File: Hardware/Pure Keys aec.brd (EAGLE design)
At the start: 97.8 x 98.7 mm, 58 parts, among them IC1 TL074P, IC2 TL072P, IC5 TL074P, Q2 20MHz, T1 2N3904, U2 LM4040A50IDBZT, U3 328P

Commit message: Slight update
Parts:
- removed U$6, U$7: PB6149L-5, INSTRUO:PB6149L
- added BUT1, BUT2: PB6149L-5, INSTRUO:PB6149L
- moved C10 60.8 mm to (20.3, 53.3)
- moved C18 45.8 mm to (29.2, 49.5)
- moved C7 44.5 mm to (86.4, 50.8), turned to 0 degrees
- moved C8 42.6 mm to (82.5, 50.8)
- moved Q2 39.9 mm to (31.8, 43.2), turned to 0 degrees
- moved U3 38.6 mm to (41.9, 58.4)
- moved C5 37.5 mm to (67.3, 34.3), turned to 0 degrees
- moved U$1 35.7 mm to (80.0, 43.2)
- moved C16 34.1 mm to (24.1, 49.5)
- moved C14 33.0 mm to (47.0, 78.7)
- moved C13 30.6 mm to (50.8, 78.7)
- moved C17 29.3 mm to (33.0, 49.5)
- moved R20 29.3 mm to (26.7, 82.5), turned to 0 degrees
- moved IC5 29.2 mm to (80.0, 27.9)
- moved C12 28.5 mm to (20.3, 64.8)
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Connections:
- removed net +UB: V1.16, V2.16
- removed net -UB: V1.8, V2.8
- removed net CLK_OUT: U3.14
- removed net MK5: V2.14
- net 5V: now also BUT1.3, BUT1.4, BUT2.3, BUT2.4, V1.16, V2.16; no longer U$6.3, U$6.4, U$7.3, U$7.4
- net BUT1: now also BUT1.1, BUT1.2; no longer U$7.1, U$7.2
- net BUT2: now also BUT2.1, BUT2.2; no longer U$6.1, U$6.2
- net BUTLED1: now also BUT1.A, U3.14; no longer U$7.A
- net BUTLED2: now also BUT2.A; no longer U$6.A
- net GND: now also V1.8, V2.14, V2.8
- net N$65: now also BUT1.K; no longer U$7.K
- net N$8: now also BUT2.K; no longer U$6.K
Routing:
- net CLK_IN: track 37.9 -> 102.1 mm
- net MOSI: track 146.7 -> 103.6 mm, vias 2 -> 0
- net POT2: track 25.3 -> 67.2 mm, vias 0 -> 1
- net BUTLED1: track 0.00 -> 39.1 mm
- net POT1: track 41.2 -> 78.7 mm
- net N$7: track 35.6 -> 69.2 mm
- net +UB: track 33.1 -> 0.00 mm
- net -UB: track 32.5 -> 0.00 mm
- net N$4: track 43.5 -> 74.6 mm
- net 5V: track 476.7 -> 505.4 mm
- net TRIG4: track 57.6 -> 29.2 mm, vias 0 -> 1
- net A1OUT: track 98.3 -> 71.7 mm, vias 1 -> 2
- net A2OUT: track 98.9 -> 74.0 mm
- net T6: track 55.6 -> 79.2 mm, vias 0 -> 2
- net N$36: track 17.5 -> 40.1 mm
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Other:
- board size 97.8 x 98.7 mm -> 99 x 98.7 mm

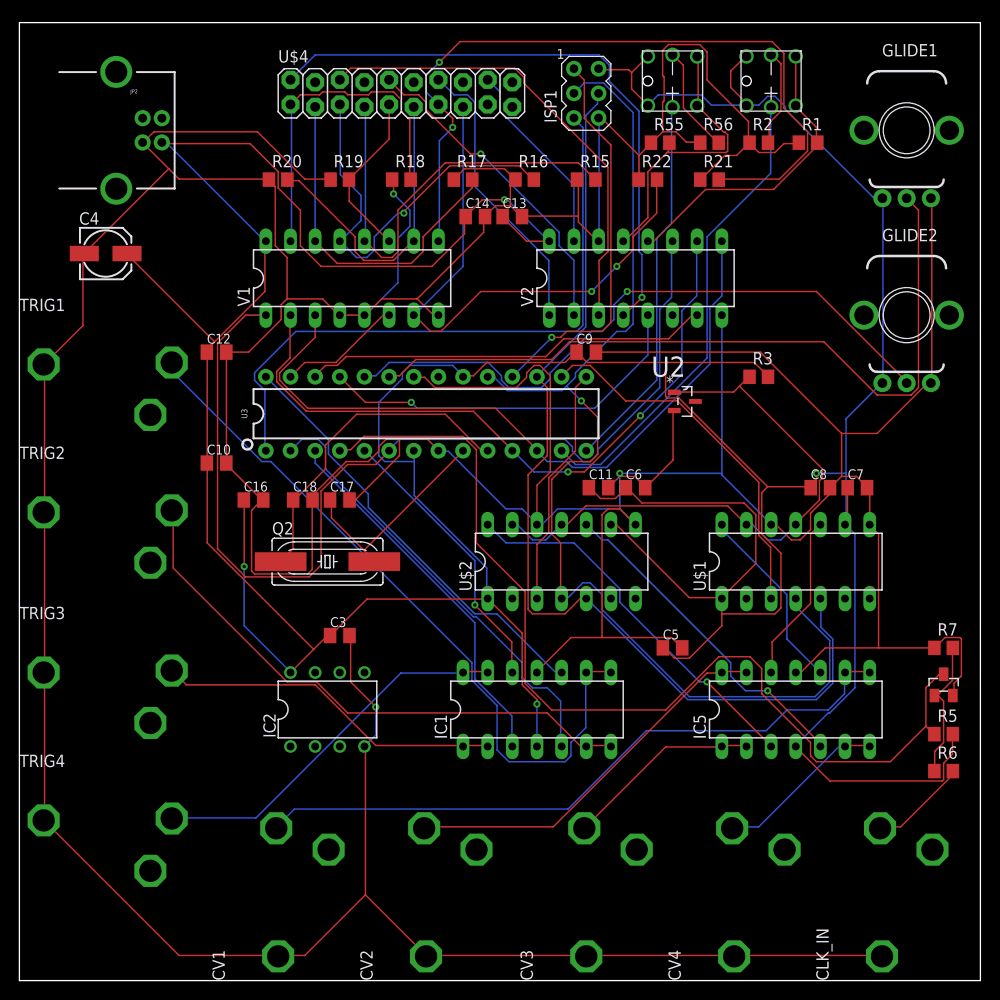
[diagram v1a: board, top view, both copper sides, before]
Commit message: Changed MUX/DEMUX connections and removed one POT
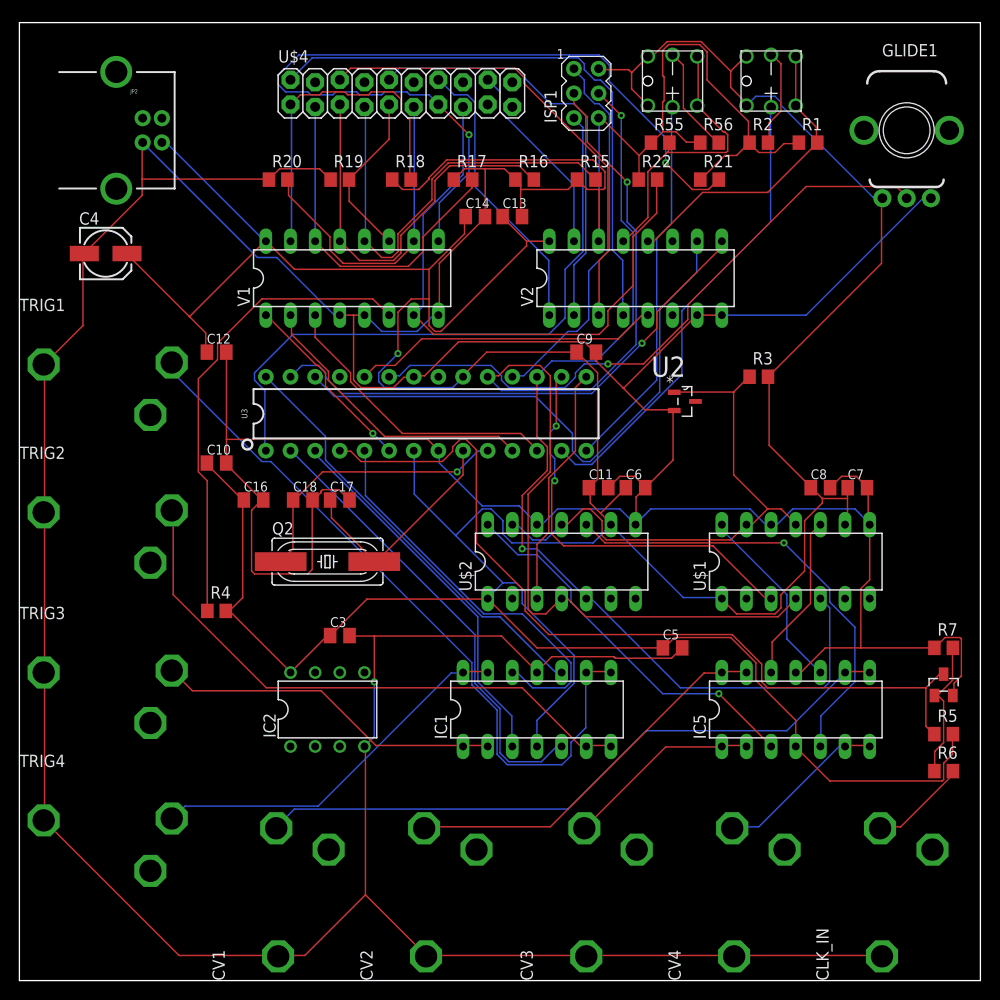
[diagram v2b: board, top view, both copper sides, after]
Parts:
- removed GLIDE2: rate, GMSN:POT
- added R4: 10K, rcl:R0805
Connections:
- removed net ENIN: U3.26, V2.7
- removed net POT2: GLIDE2.P$2, U3.24
- new net A0IN: U3.25
- new net A1IN: U3.26, V2.10
- new net A2IN: U3.27, V2.9
- new net AOIN: V2.11
- net 5V: now also R4.2; no longer GLIDE2.P$1
- net A0OUT: no longer V2.11
- net A1OUT: no longer V2.10
- net A2OUT: no longer V2.9
- net DAIN: now also U3.24; no longer U3.25
- net ENOUT: now also R4.1; no longer U3.27
- net GND: now also V2.7; no longer GLIDE2.P$3
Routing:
- net A0OUT: track 104.9 -> 19.3 mm, vias 0 -> 1
- net POT2: track 67.2 -> 0.00 mm, vias 1 -> 0
- net A1IN: track 0.00 -> 60.4 mm
- net 5V: track 505.4 -> 450.1 mm, vias 4 -> 1
- net A2IN: track 0.00 -> 54.2 mm, vias 0 -> 1
- net A2OUT: track 74.0 -> 30.6 mm
- net ENIN: track 42.1 -> 0.00 mm
- net A1OUT: track 71.7 -> 30.4 mm, vias 2 -> 0
- net ENOUT: track 12.8 -> 49.1 mm
- net GND: track 726.0 -> 700.2 mm, vias 3 -> 1
- net CLK_IN: track 102.1 -> 88.1 mm
- net POT1: track 78.7 -> 65.4 mm, vias 0 -> 1
- net TRIG4: track 29.2 -> 41.9 mm, vias 1 -> 0
- net VOUTD: track 34.6 -> 46.6 mm
- net T6: track 79.2 -> 90.5 mm
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
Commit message: added back plane
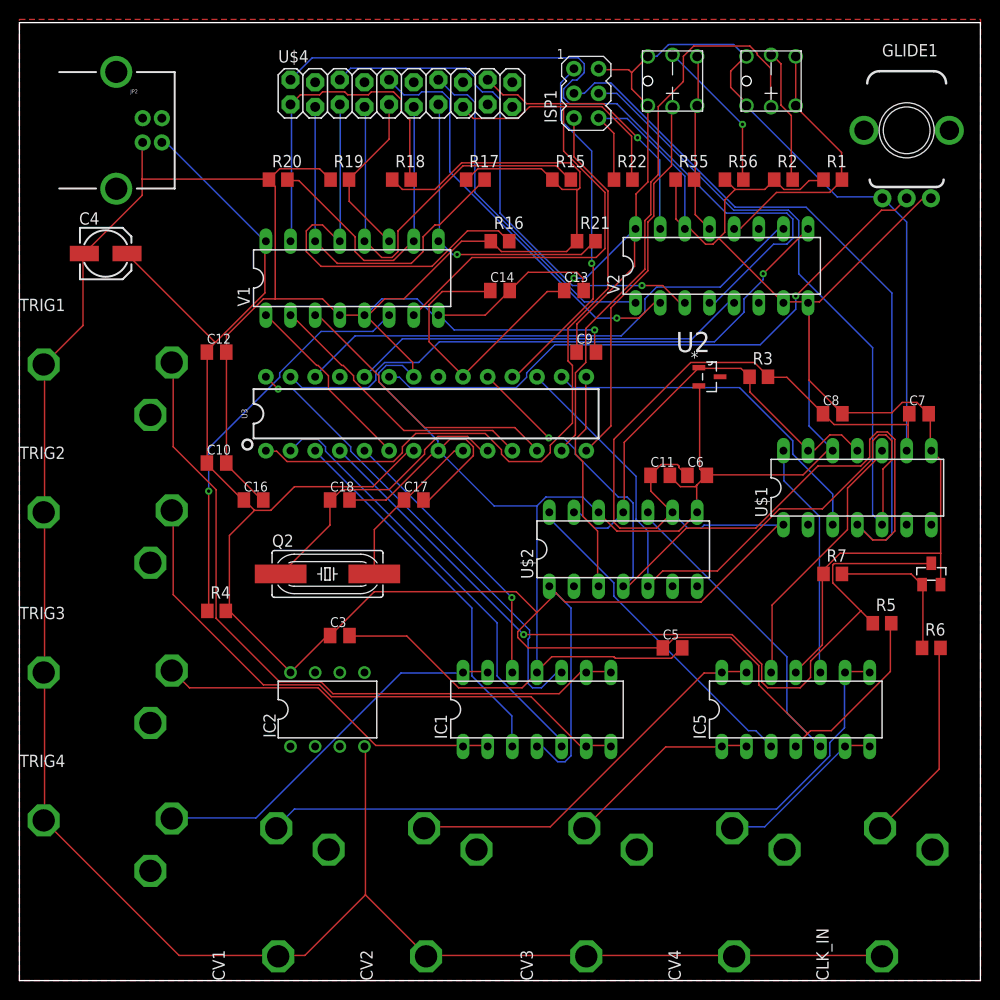
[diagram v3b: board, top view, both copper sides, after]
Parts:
- moved R21 14.2 mm to (58.4, 76.2)
- moved R7 13.7 mm to (83.8, 41.9)
- moved R5 13.1 mm to (88.9, 36.8)
- moved R6 12.8 mm to (94.0, 34.3)
- moved T1 11.5 mm to (94.0, 41.9)
- moved C7 9.92 mm to (92.7, 58.4)
- moved U$1 9.92 mm to (86.4, 50.8)
- moved C13 9.92 mm to (57.1, 71.1)
- moved V2 8.98 mm to (72.4, 73.7)
- moved C14 8.03 mm to (49.5, 71.1)
- moved C8 7.73 mm to (83.8, 58.4)
- moved C17 7.62 mm to (40.6, 49.5)
- moved R16 6.84 mm to (49.5, 76.2)
- moved C11 6.48 mm to (66.0, 52.1)
- moved C6 6.48 mm to (69.8, 52.1)
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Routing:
- net T6: track 90.5 -> 31.5 mm, vias 2 -> 1
- net SCK: track 108.8 -> 151.4 mm
- net MOSI: track 103.6 -> 129.3 mm, vias 2 -> 0
- net MK0: track 59.4 -> 78.3 mm
- net VOUTD: track 46.6 -> 31.5 mm, vias 1 -> 0
- net TRIG4: track 41.9 -> 29.2 mm, vias 0 -> 1
- net BUTLED2: track 48.2 -> 60.4 mm
- net N$26: track 10.1 -> 21.3 mm
- net BUT1: track 29.8 -> 18.8 mm
- net 3VREF: track 57.4 -> 46.8 mm
- net 5V: track 450.1 -> 460.4 mm
- net VOUTB: track 17.4 -> 27.6 mm
- net DAIN: track 31.8 -> 41.3 mm
- net A2IN: track 54.2 -> 62.3 mm
- net MK4: track 20.3 -> 28.3 mm, vias 0 -> 1
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- added copper zone on layer 1, net N$1

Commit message: added back plane
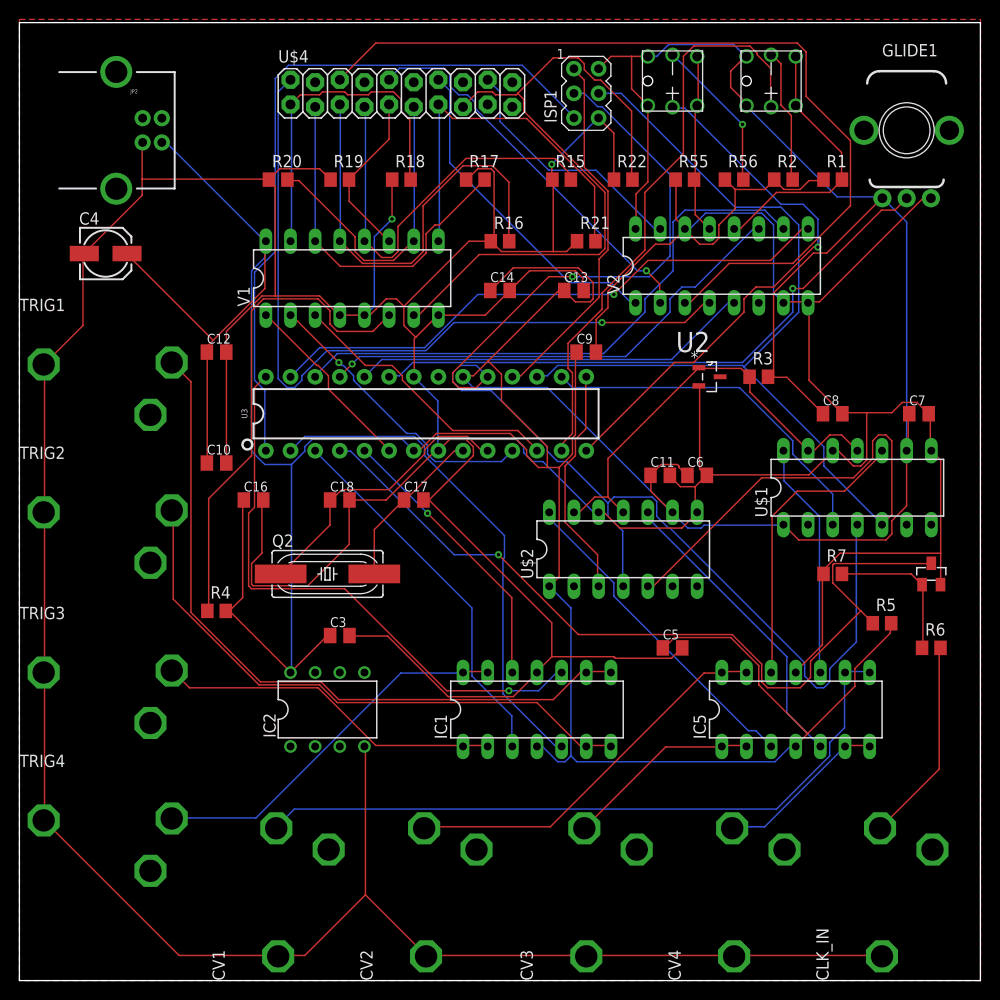
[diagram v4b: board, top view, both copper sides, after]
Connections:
- removed net AOIN: V2.11
- net A0IN: now also V2.11
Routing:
- net A0IN: track 0.00 -> 50.3 mm, vias 0 -> 1
- net 5V: track 460.4 -> 509.1 mm, vias 1 -> 0
- net MK1: track 53.5 -> 89.1 mm, vias 1 -> 0
- net BUTLED1: track 39.1 -> 56.0 mm, vias 0 -> 1
- net TRIG1: track 48.1 -> 59.8 mm
- net SCK: track 151.4 -> 141.0 mm
- net ENOUT: track 41.4 -> 50.5 mm, vias 1 -> 0
- net T7: track 63.2 -> 71.8 mm
- net T6: track 31.5 -> 39.6 mm, vias 1 -> 0
- net TRIG2: track 45.4 -> 52.1 mm
- net A1IN: track 55.4 -> 60.0 mm
- net VOUTB: track 27.6 -> 30.5 mm
- net MK2: track 43.4 -> 40.7 mm
- net GND: track 697.6 -> 694.9 mm, vias 1 -> 2
- net A2IN: track 62.3 -> 59.7 mm
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- added copper zone on layer 1, net GND
- removed copper zone on layer 1, net N$1
